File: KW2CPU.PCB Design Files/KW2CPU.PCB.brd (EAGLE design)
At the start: 44 x 30 mm, 80 parts, among them IC1 25AA080SN, J1 DF12_M, U1 MKW21D, U3 RF6555, X1 32KHZ, X2 32MHZ

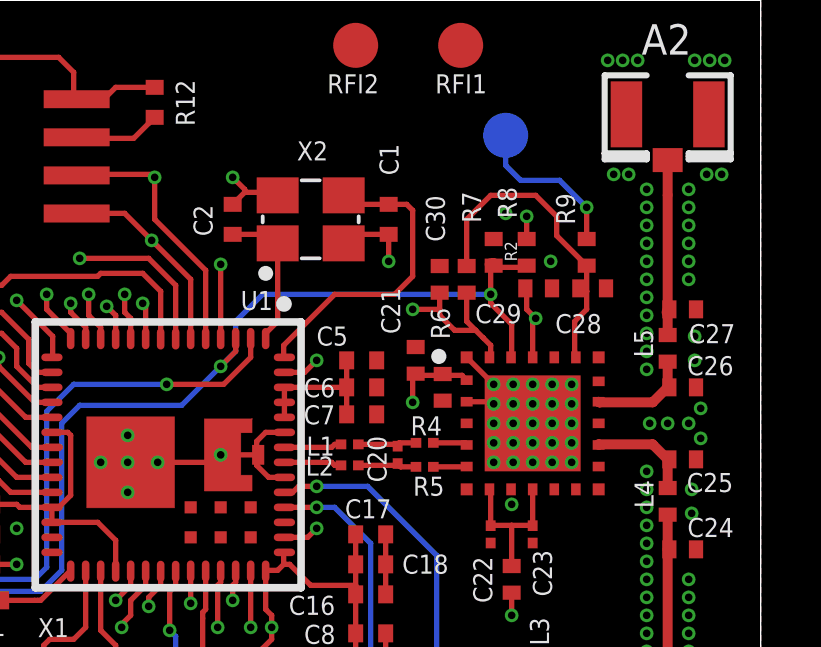
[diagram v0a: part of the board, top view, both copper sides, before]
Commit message: Fixes after Rafael's review
* DNP all but the dedicated RX/TX antenna select option via GPIO2.
* DNP all but the LNA passthrough control option.
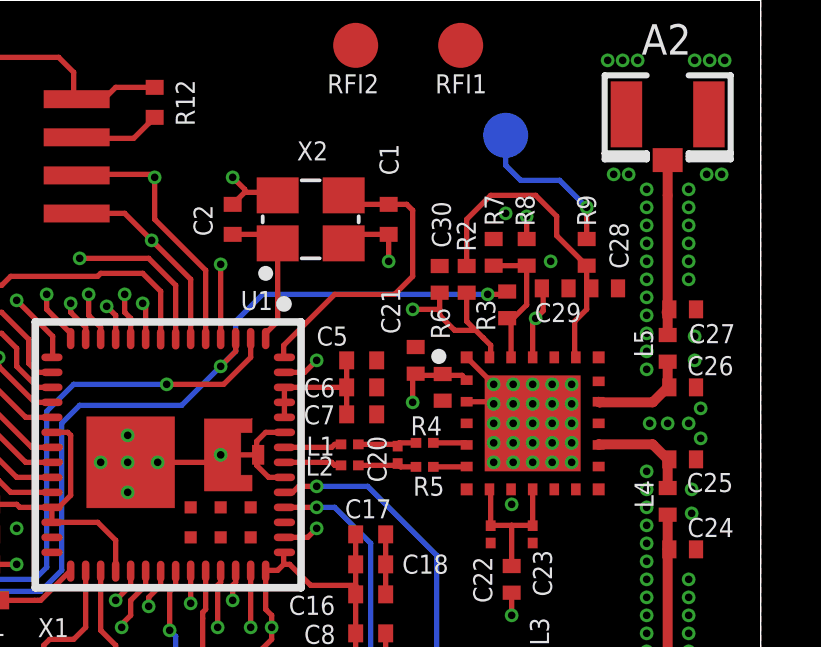
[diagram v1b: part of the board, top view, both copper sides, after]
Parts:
- added R3: 0, GW-devices:RFMD0402
- moved C29 0.55 mm to (28.6, 5.40)
- moved C28 0.40 mm to (30.3, 5.40)
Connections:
- new net N$8: R3.P$2, R7.P$1, R8.P$2, U3.P$23
- net GPIO2: now also R3.P$1; no longer R7.P$1, R8.P$2, U3.P$23
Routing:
- net N$8: track 0.00 -> 4.73 mm
- net GPIO2: track 39.3 -> 35.4 mm

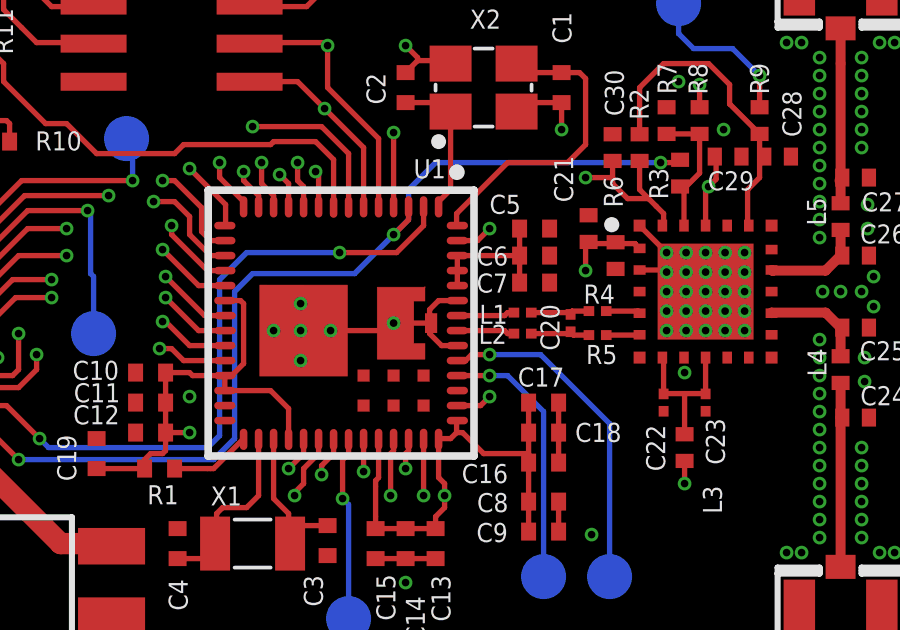
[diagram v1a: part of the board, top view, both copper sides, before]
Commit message: Connect RF6555 CE to KW2 AREG
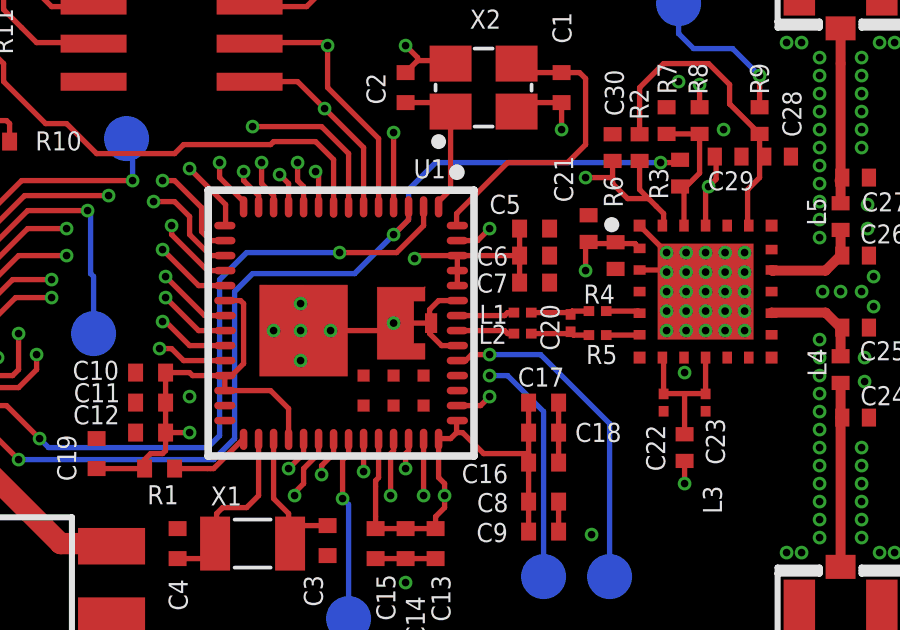
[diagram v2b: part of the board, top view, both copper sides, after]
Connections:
- removed net N$6: C5.1, C6.1, C7.1, U1.P$52, U1.P$53, U1.P$54
- removed net RX_SWITCH: C21.P$1, R6.P$1, TP7.TP, U1.P$46, U3.P$2
- new net RADIO_AREG: C21.P$1, C5.1, C6.1, C7.1, R6.P$1, TP7.TP, U1.P$52, U1.P$53, U1.P$54, U3.P$2
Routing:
- net RADIO_AREG: track 0.00 -> 36.4 mm, vias 0 -> 3
- net RX_SWITCH: track 30.1 -> 0.00 mm, vias 2 -> 0
- net N$6: track 5.86 -> 0.00 mm
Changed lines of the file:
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@@
 <wire x1="19.6" y1="3.1" x2="19.6" y2="3.5" width="0.1778" layer="1"/>
-</signal>
-<signal name="N$6">
-<contactref element="U1" pad="P$54"/>
-<contactref element="U1" pad="P$53"/>
-<contactref element="U1" pad="P$52"/>
-<contactref element="C7" pad="1"/>
-<contactref element="C6" pad="1"/>
-<contactref element="C5" pad="1"/>
-<wire x1="21.7" y1="3" x2="21.7" y2="2.2" width="0.1778" layer="1"/>
-<wire x1="21.7" y1="2.2" x2="21.7" y2="2.1" width="0.1778" layer="1"/>
-<wire x1="21.7" y1="2.1" x2="21.7" y2="1.9" width="0.1778" layer="1"/>
-<wire x1="21.7" y1="1.9" x2="21.7" y2="1.2" width="0.1778" layer="1"/>
-<wire x1="19.625" y1="2.1" x2="19.625" y2="1.6" width="0.1778" layer="1"/>
-<wire x1="19.625" y1="1.6" x2="19.625" y2="1.1" width="0.1778" layer="1"/>
-<wire x1="19.625" y1="2.1" x2="21.7" y2="2.1" width="0.1778" layer="1"/>
-<wire x1="21.7" y1="2.1" x2="21.6" y2="2.2" width="0.1778" layer="1"/>
-<wire x1="21.6" y1="2.2" x2="21.7" y2="2.1" width="0.1778" layer="1"/>
-<wire x1="21.7" y1="2.1" x2="21.7" y2="1.9" width="0.1778" layer="1"/>
-<wire x1="21.7" y1="1.9" x2="21.7" y2="2.1" width="0.1778" layer="1"/>
-<wire x1="21.7" y1="2.1" x2="21.7" y2="2.2" width="0.1778" layer="1"/>
-<wire x1="21.7" y1="2.2" x2="21.6" y2="2.2" width="0.1778" layer="1"/>
-<wire x1="21.6" y1="2.2" x2="21.7" y2="2.2" width="0.1778" layer="1"/>
 </signal>
 <signal name="+3V3">
@@
 <wire x1="26.5" y1="3.14" x2="26.46" y2="3.1" width="0.1778" layer="1"/>
 </signal>
-<signal name="RX_SWITCH">
+<signal name="RADIO_AREG">
 <contactref element="C21" pad="P$1"/>
 <contactref element="R6" pad="P$1"/>
 <contactref element="U3" pad="P$2"/>
-<contactref element="U1" pad="P$46"/>
 <wire x1="25.55" y1="2.5" x2="24.9" y2="2.5" width="0.1778" layer="1"/>
 <wire x1="24.9" y1="2.5445" x2="24.9" y2="2.5" width="0.1778" layer="1"/>
 <wire x1="24.9" y1="2.5" x2="24" y2="2.5" width="0.1778" layer="1"/>
 <wire x1="24" y1="2.5" x2="24" y2="2.5555" width="0.1778" layer="1"/>
-<wire x1="19.625" y1="-1.9" x2="20.7" y2="-1.9" width="0.1778" layer="1"/>
 <via x="20.7" y="-1.9" extent="1-16" drill="0.254"/>
 <wire x1="20.7" y1="-1.9" x2="19.2" y2="-1.9" width="0.1778" layer="15"/>
 <wire x1="19.2" y1="-1.9" x2="18.2" y2="-0.9" width="0.1778" layer="15"/>
-<wire x1="18.2" y1="-0.9" x2="18.2" y2="3" width="0.1778" layer="15"/>
+<wire x1="18.2" y1="-0.9" x2="18.2" y2="2" width="0.1778" layer="15"/>
+<wire x1="18.2" y1="2" x2="18.2" y2="3" width="0.1778" layer="15"/>
 <wire x1="24" y1="2.5" x2="23.9" y2="2.4" width="0.1778" layer="1"/>
 <wire x1="23.9" y1="2.4" x2="23.9" y2="1.6" width="0.1778" layer="1"/>
@@
 <wire x1="25.55" y1="2.5" x2="25.55" y2="2.49" width="0.1778" layer="1"/>
 <wire x1="25.55" y1="2.49" x2="25.7" y2="2.34" width="0.1778" layer="1"/>
+<contactref element="U1" pad="P$54"/>
+<contactref element="U1" pad="P$53"/>
+<contactref element="U1" pad="P$52"/>
+<contactref element="C7" pad="1"/>
+<contactref element="C6" pad="1"/>
+<contactref element="C5" pad="1"/>
+<wire x1="21.7" y1="3" x2="21.7" y2="2.2" width="0.1778" layer="1"/>
+<wire x1="21.7" y1="2.2" x2="21.7" y2="2.1" width="0.1778" layer="1"/>
+<wire x1="21.7" y1="2.1" x2="21.7" y2="1.9" width="0.1778" layer="1"/>
+<wire x1="21.7" y1="1.9" x2="21.7" y2="1.2" width="0.1778" layer="1"/>
+<wire x1="19.625" y1="2.1" x2="19.625" y2="1.6" width="0.1778" layer="1"/>
+<wire x1="19.625" y1="1.6" x2="19.625" y2="1.1" width="0.1778" layer="1"/>
+<wire x1="19.625" y1="2.1" x2="21.7" y2="2.1" width="0.1778" layer="1"/>
+<wire x1="21.7" y1="2.1" x2="21.6" y2="2.2" width="0.1778" layer="1"/>
+<wire x1="21.6" y1="2.2" x2="21.7" y2="2.1" width="0.1778" layer="1"/>
+<wire x1="21.7" y1="2.1" x2="21.7" y2="1.9" width="0.1778" layer="1"/>
+<wire x1="21.7" y1="1.9" x2="21.7" y2="2.1" width="0.1778" layer="1"/>
+<wire x1="21.7" y1="2.1" x2="21.7" y2="2.2" width="0.1778" layer="1"/>
+<wire x1="21.7" y1="2.2" x2="21.6" y2="2.2" width="0.1778" layer="1"/>
+<wire x1="21.6" y1="2.2" x2="21.7" y2="2.2" width="0.1778" layer="1"/>
+<wire x1="19.625" y1="2.1" x2="18.3" y2="2.1" width="0.1776" layer="1"/>
+<wire x1="18.3" y1="2.1" x2="18.2" y2="2" width="0.1776" layer="1"/>
+<via x="18.2" y="2" extent="1-16" drill="0.254"/>
 </signal>
 <signal name="EXTAL32">

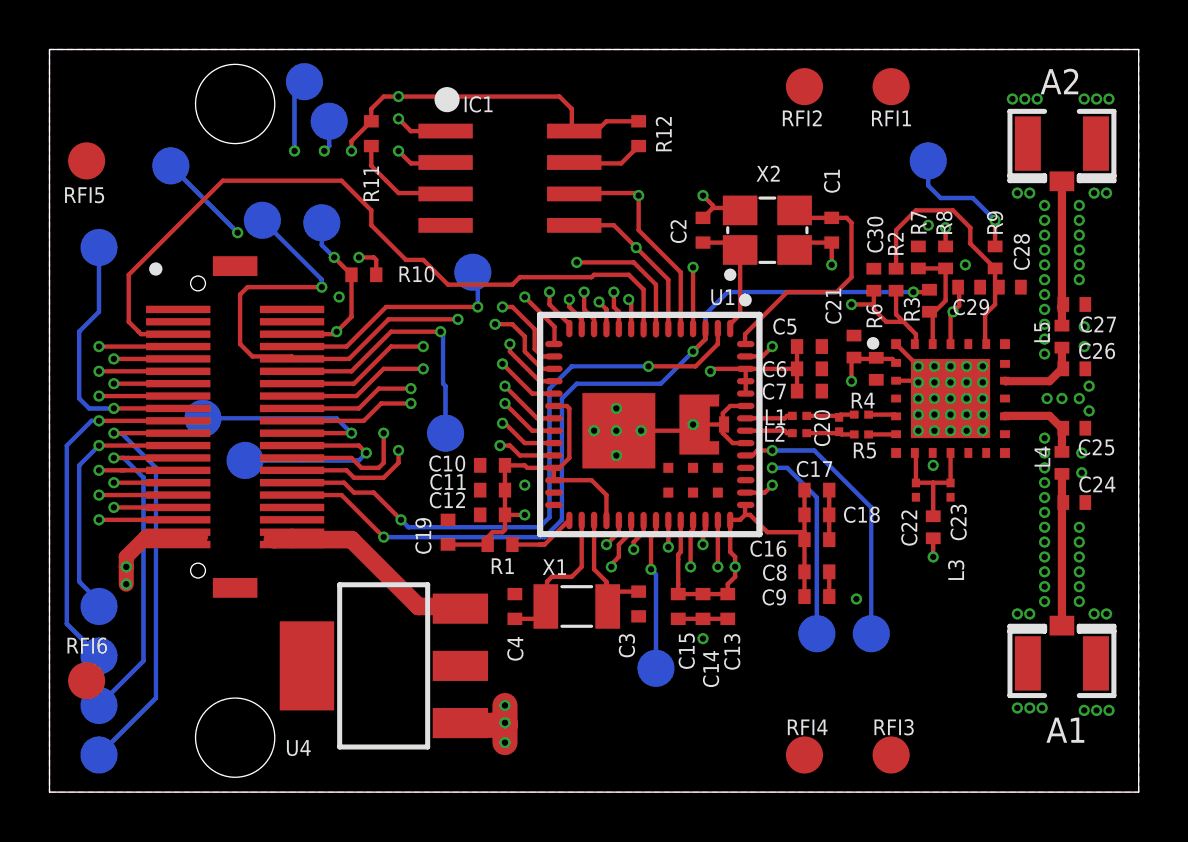
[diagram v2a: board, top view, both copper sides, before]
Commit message: Fixed grid units, adjusted vias
Moved and adjusted all GND vias near RF traces
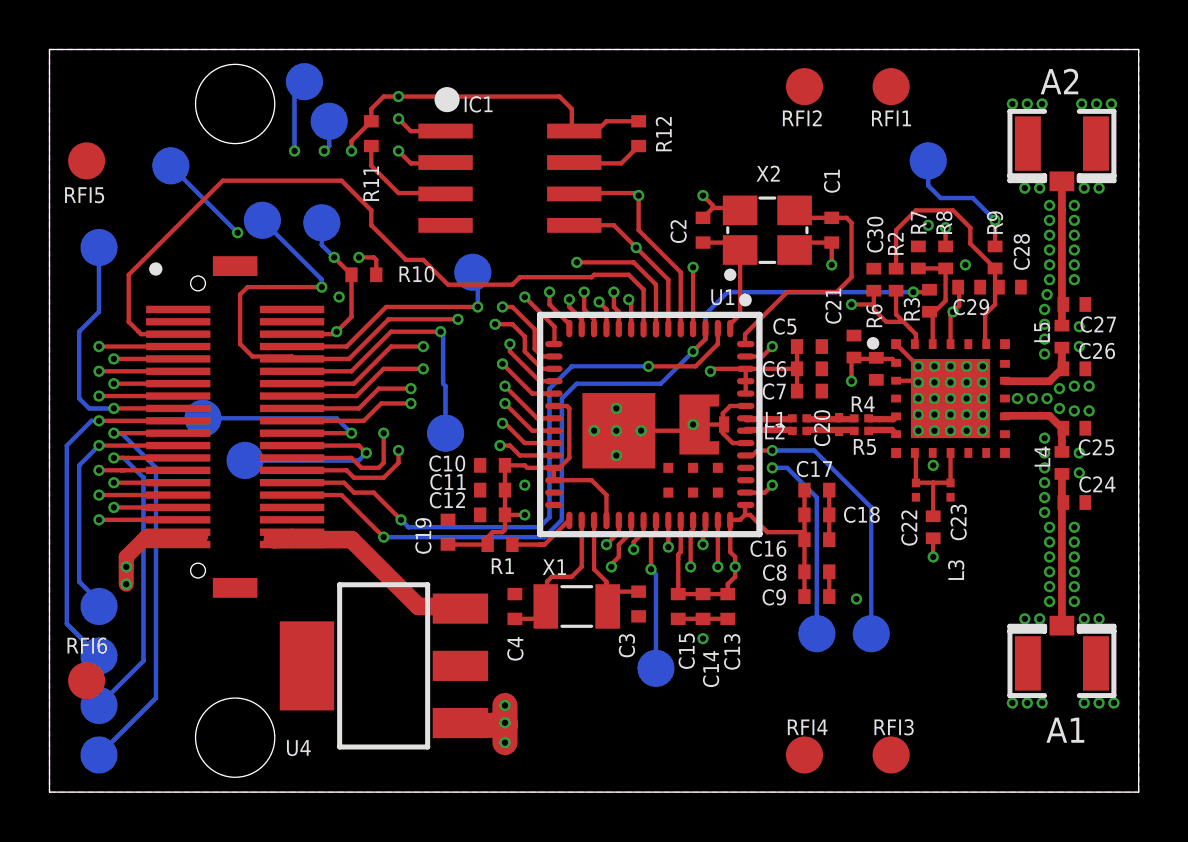
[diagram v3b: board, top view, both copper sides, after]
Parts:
- moved R4 0.15 mm to (24.3, 0.10)
- moved R5 0.14 mm to (24.3, -0.41)
- moved L1 0.10 mm to (21.8, 0.10)
- moved L2 0.09 mm to (21.8, -0.41)
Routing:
- net GND: vias 104 -> 108

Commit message: Updated traces for impedance
As per RoyalCircuits recommendation
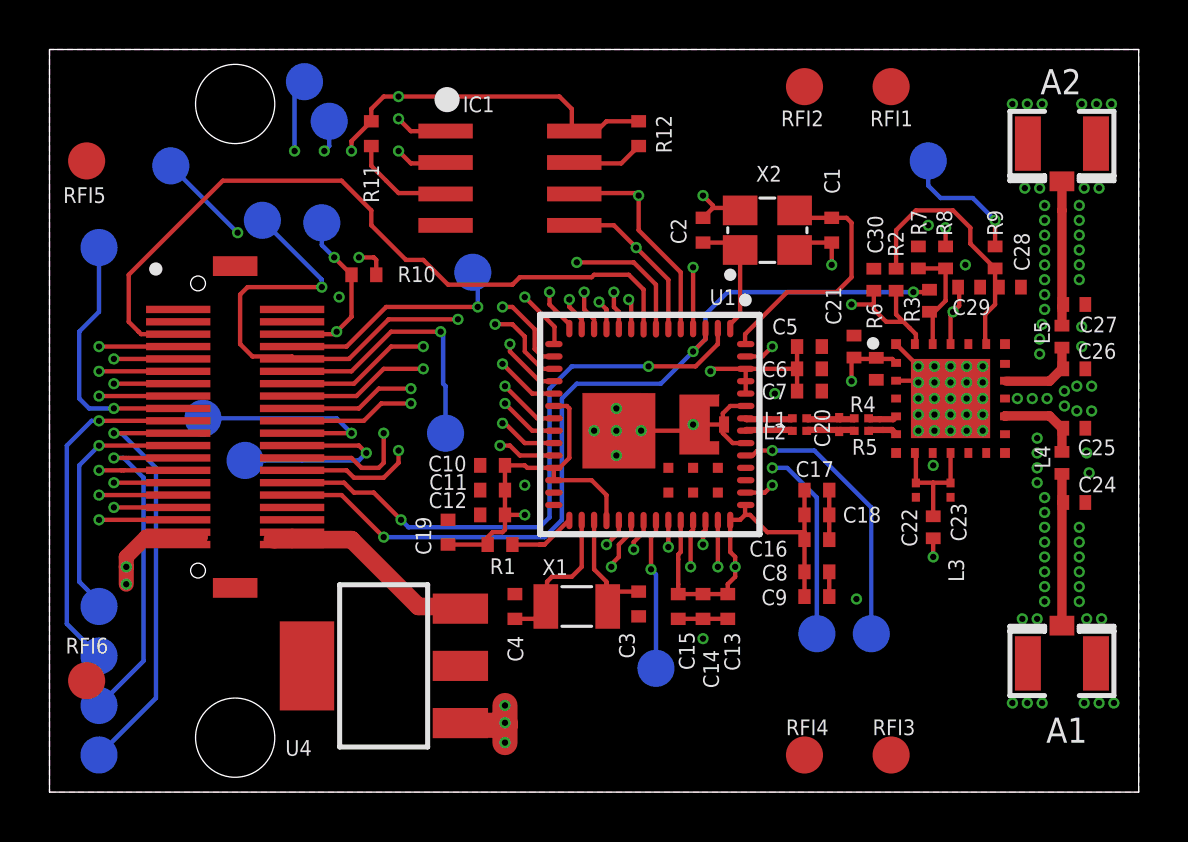
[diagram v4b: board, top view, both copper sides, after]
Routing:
- net GND: vias 108 -> 109

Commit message: Minor adjustments (silkscreen, DNPs)
Added silkscren RefDes for antenna connectors, RFMD and Hirose
connector. Added PN for antenna connector, DNP for match neworks and
re-exported CSV BOM
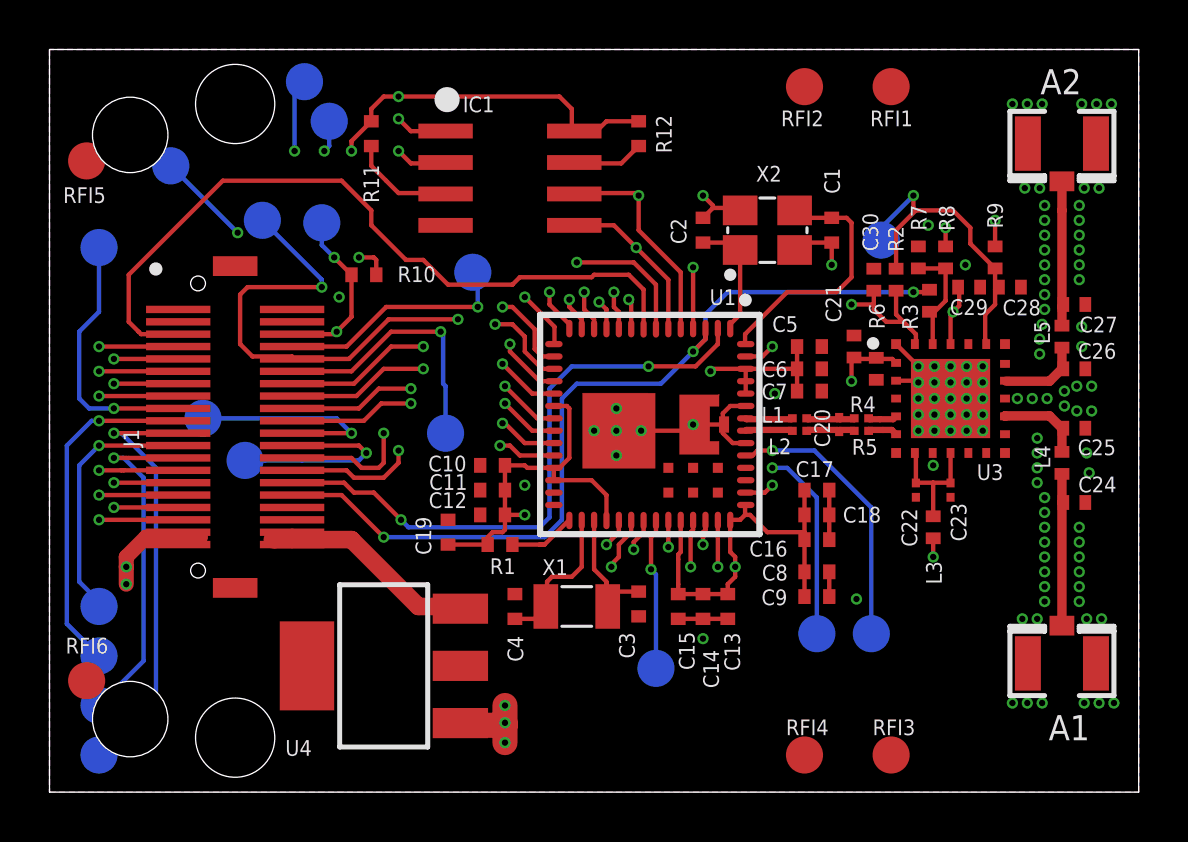
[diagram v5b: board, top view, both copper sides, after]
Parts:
- moved TP8 3.72 mm to (25.1, 7.30)
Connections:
- net ANTSEL: now also TP8.TP
- net ANT_A: no longer TP8.TP
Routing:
- net ANT_A: track 31.4 -> 27.1 mm
- net ANTSEL: track 10.7 -> 13.7 mm, vias 0 -> 1
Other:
- board text added: "7/31/15"

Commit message: KW2CPU.PCB.v1.3P1
Design and production files for new KW2
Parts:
- removed RFI1, RFI2, RFI3, RFI4, RFI5, RFI6: PTR1TP15R, testpad:TP15R
- A1, A2: value (none) -> 50Ohm
- C25: value 0.0pF -> 0.2pF
- L4: value 1.2nH -> 2.2nH
- R10: value 10K -> 10k
- U4: value (none) -> 3.3V
- X1: value 32KHZ -> 32.768kHz
- moved U4 1.46 mm to (5.40, -8.50)
- moved C19 0.81 mm to (7.70, -3.70)
- moved J1 0.25 mm to (-1.00, 0.00)
- moved L1 0.20 mm to (22.0, 0.10)
- moved L2 0.20 mm to (22.0, -0.41)
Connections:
- net GND: no longer RFI1.TP, RFI2.TP, RFI3.TP, RFI4.TP, RFI5.TP, RFI6.TP
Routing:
- net PTD4/LLWU_P14/MADC0_SE21/SPI0_PCS1/!UART0_RTS!/FTM0_CH4/EWM_IN/GPIO_BSM_FRAME: track 52.7 -> 42.4 mm
- net +3V3: track 66.4 -> 73.0 mm
- net GND: track 19.4 -> 16.8 mm, vias 109 -> 108
- net PTD1/ADC0_SE5B/SPI0_SCK/!UART2_CTS: track 31.7 -> 29.7 mm
- net VIN: track 11.2 -> 10.3 mm
- net PTC5/LLWU_P9/SPI0_SCK/LPTMR0_ALT2/I2S0_RXDO/CMP0_OUT: track 35.7 -> 36.2 mm
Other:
- board text added: "8/5/15"
- board text removed: "7/31/15"
